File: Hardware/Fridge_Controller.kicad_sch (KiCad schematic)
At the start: 21 parts, among them J1 Power, J2 Compressor, J3 Temperature, K1 RZ01-1A4-D005, Q1 DMG3414U, U1 PIC12F683-IP, U2 MCP1541-TT

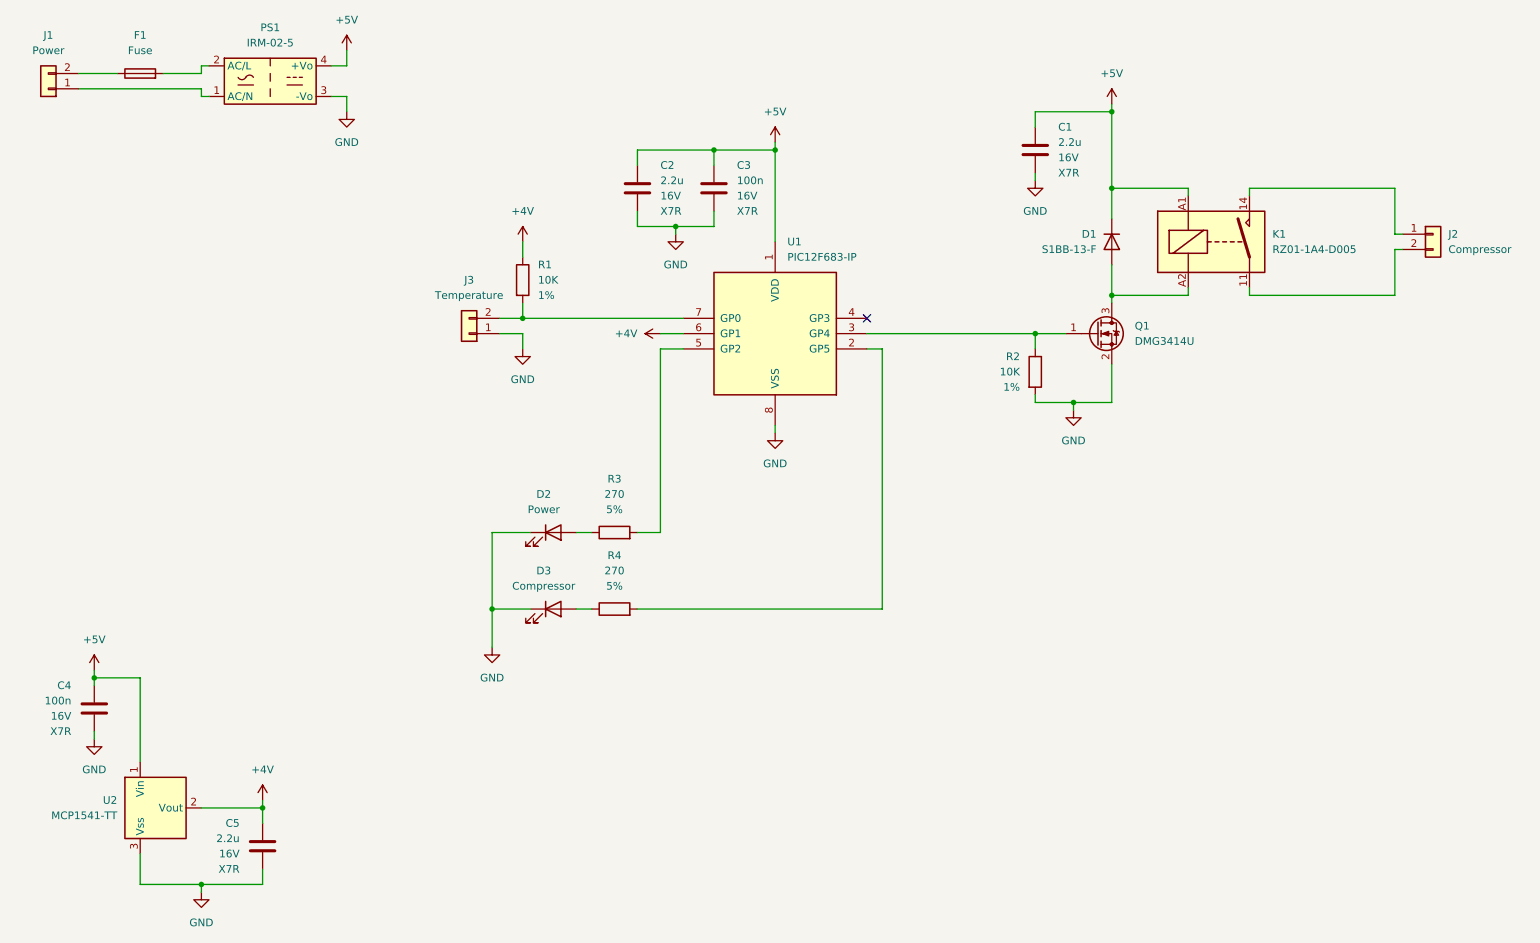
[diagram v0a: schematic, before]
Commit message: [Hardware] Added fuse, fuse holder and screw terminals part references to schematics.
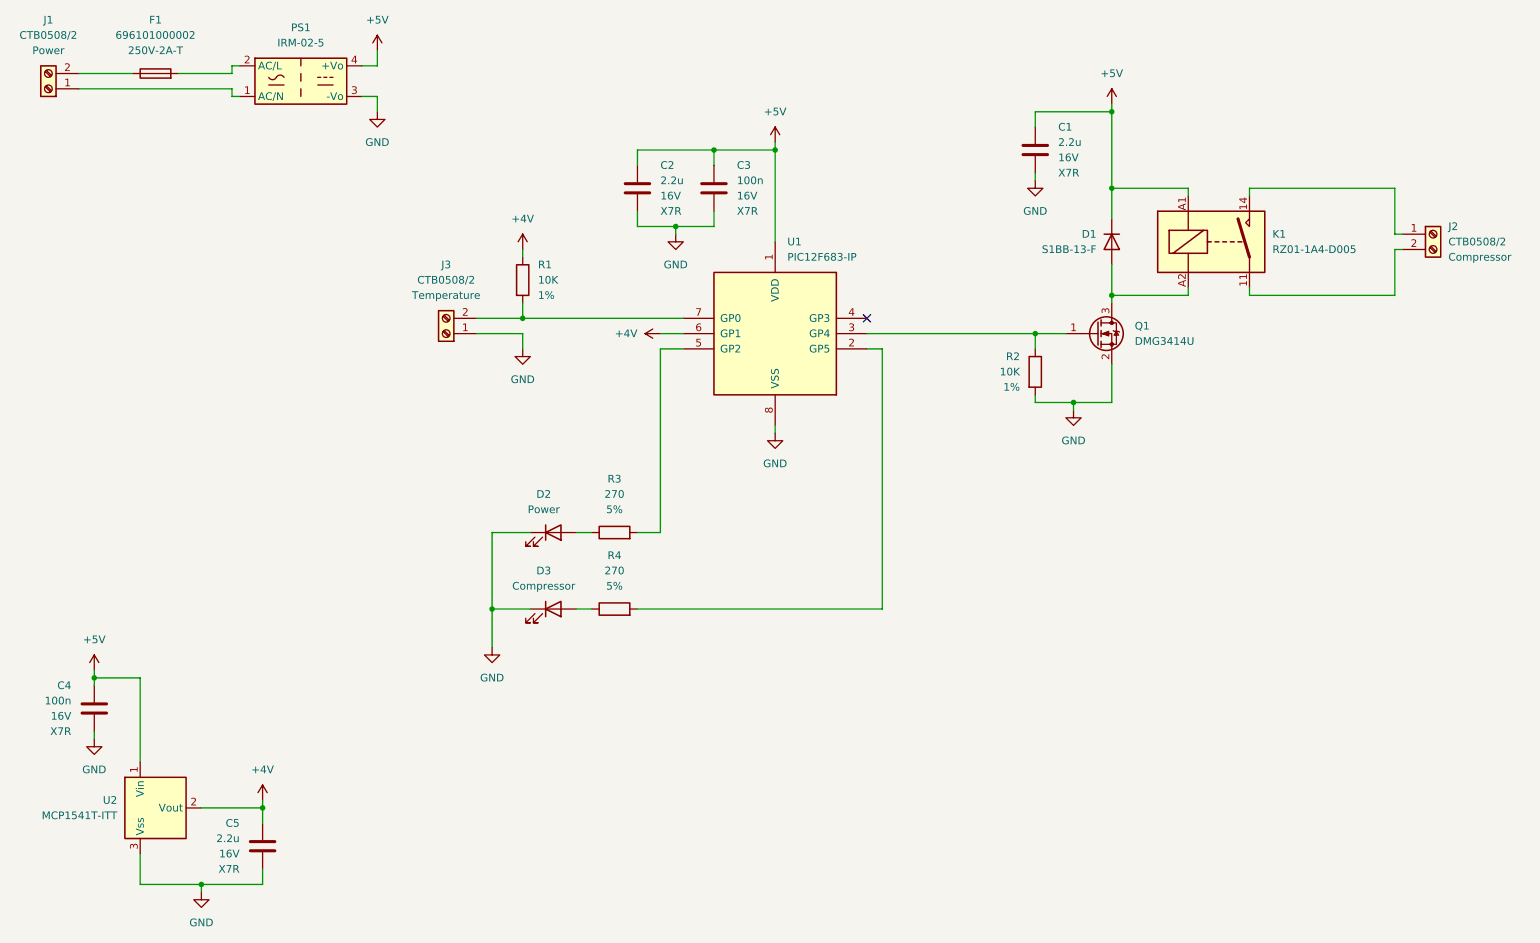
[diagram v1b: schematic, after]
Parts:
- F1: value Fuse -> 696101000002; footprint (none) -> Fuse:Fuseholder_Cylinder-5x20mm_Stelvio-Kontek_PTF78_Horizontal_Open; Manufacturer (none) -> Wurth; Value2 (none) -> 250V-2A-T
- J1: value Power -> CTB0508/2; symbol Connector_Generic:Conn_01x02 -> Connector:Screw_Terminal_01x02; Manufacturer (none) -> Camdenboss; Value2 (none) -> Power
- J2: value Compressor -> CTB0508/2; symbol Connector_Generic:Conn_01x02 -> Connector:Screw_Terminal_01x02; Manufacturer (none) -> Camdenboss; Value2 (none) -> Compressor
- J3: value Temperature -> CTB0508/2; symbol Connector_Generic:Conn_01x02 -> Connector:Screw_Terminal_01x02; Manufacturer (none) -> Camdenboss; Value2 (none) -> Temperature
- U2: value MCP1541-TT -> MCP1541T-ITT
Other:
- moved on the sheet: F1, PS1

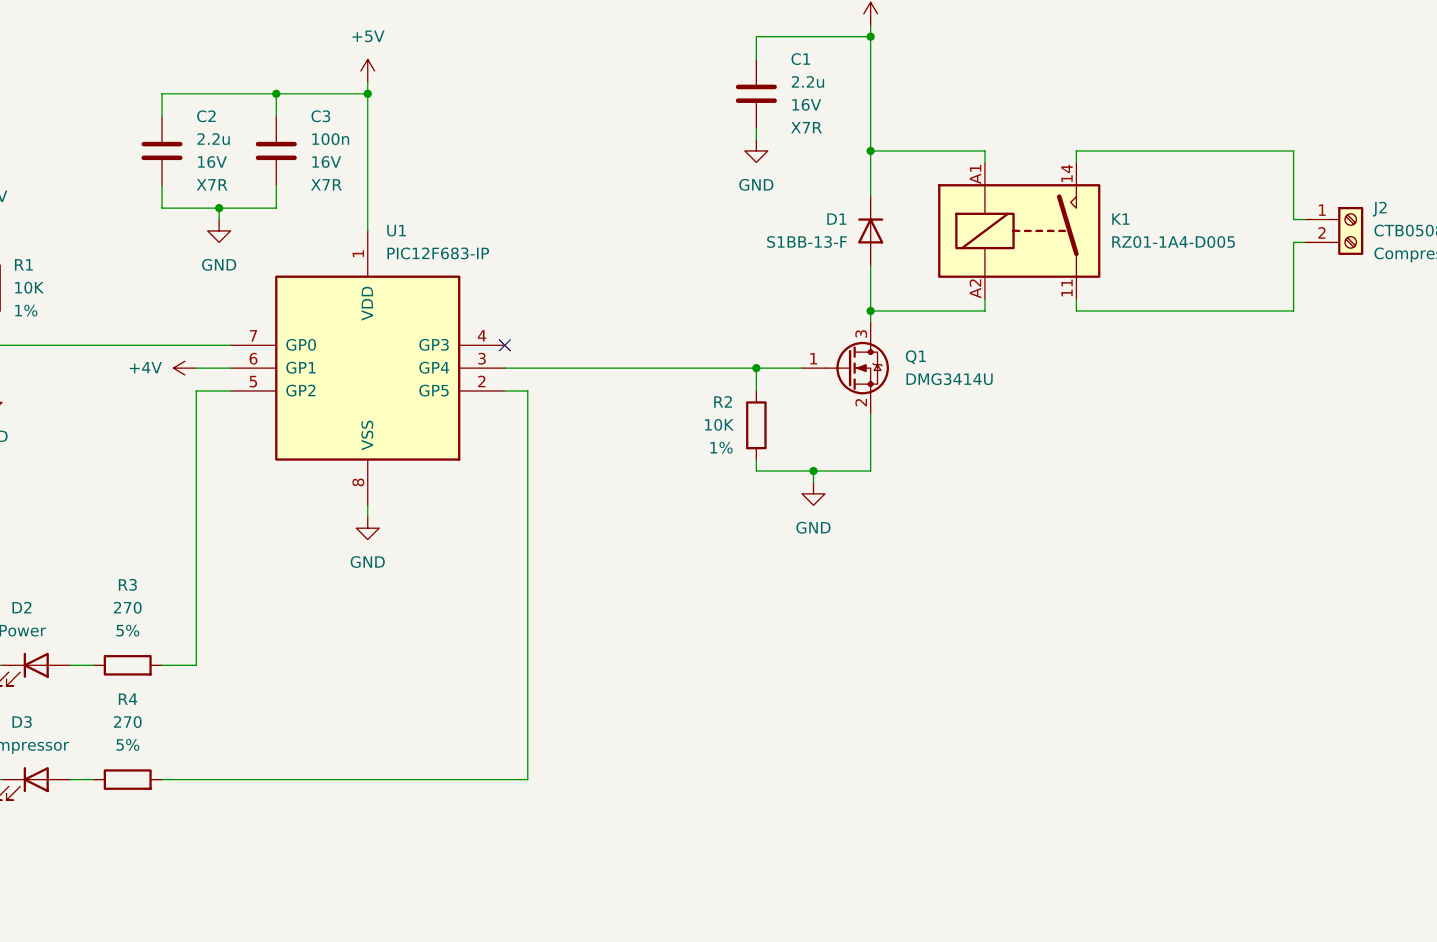
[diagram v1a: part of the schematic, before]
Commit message: [Hardware] Added a pull-up resistor on microcontroller /MCLR pin so the /MCLR signal can be left active in the MCU fuses and the MCU can be more easily reflashed when inserted on a development board.
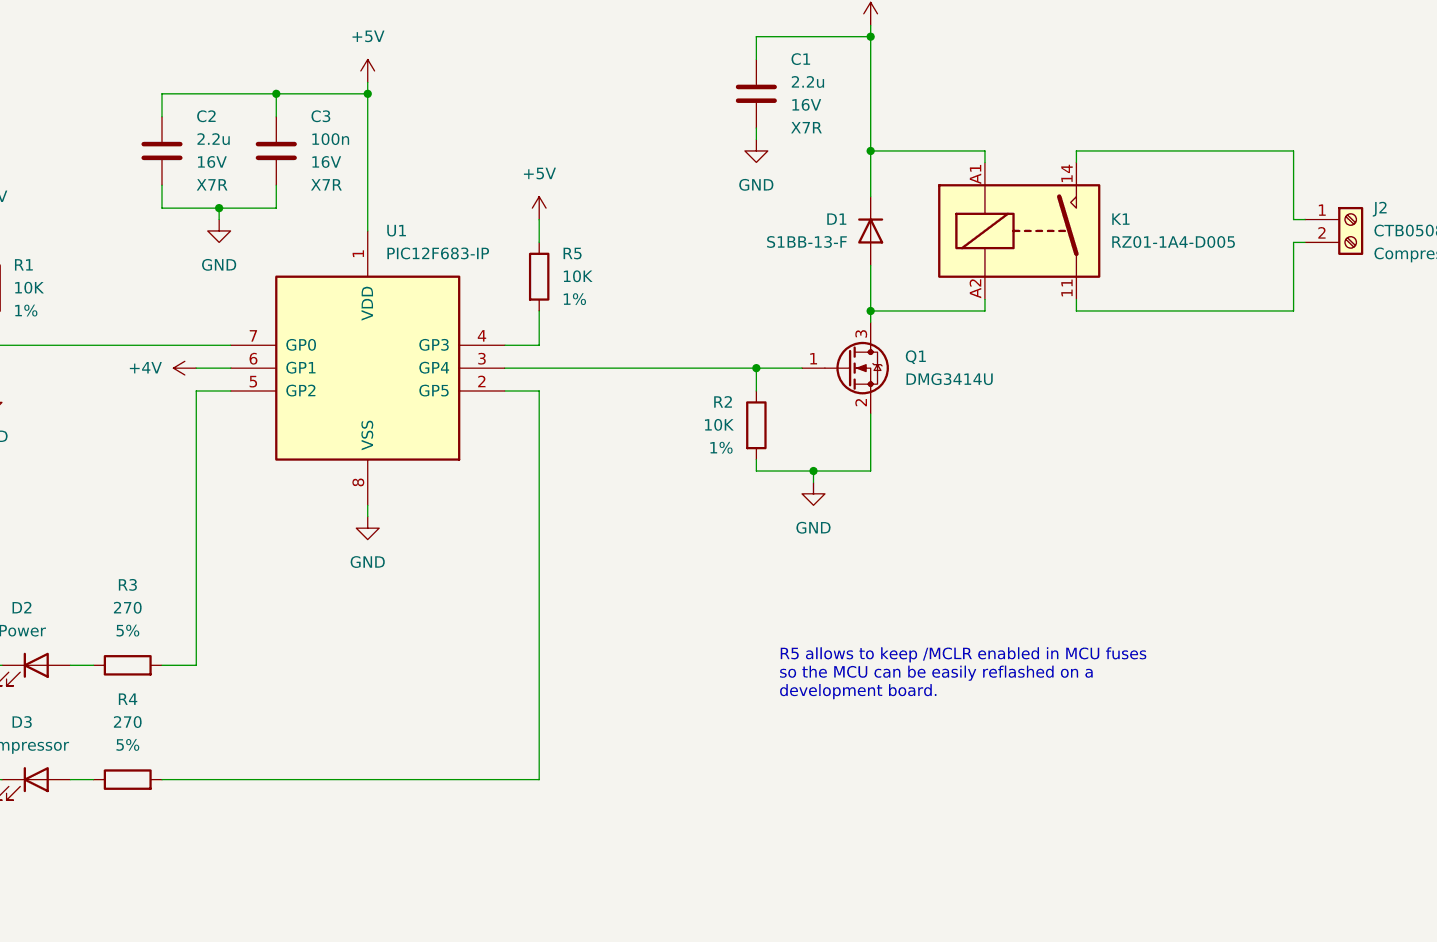
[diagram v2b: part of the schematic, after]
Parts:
- added R5: 10K, Resistor_SMD:R_0603_1608Metric_Pad0.98x0.95mm_HandSolder, symbol Device:R
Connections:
- net +5V: now also R5.1
- net at U1.4 (GP3): now also R5.2
- no-connect marks 1 -> 0
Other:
- note added: "R5 allows to keep /MCLR enabled in MCU fuses so the MCU can be easily reflashed on a development board."
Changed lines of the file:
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@@
   (junction (at 147.32 54.61) (diameter 0) (color 0 0 0 0)
   )
-  (no_connect (at 162.56 82.55))
   (wire (pts (xy 190.5 58.42) (xy 190.5 59.69))
     (stroke (width 0) (type default) (color 0 0 0 0))
@@
     (stroke (width 0) (type default) (color 0 0 0 0))
   )
-  (wire (pts (xy 162.56 87.63) (xy 165.1 87.63))
+  (wire (pts (xy 162.56 87.63) (xy 166.37 87.63))
     (stroke (width 0) (type default) (color 0 0 0 0))
   )
@@
     (stroke (width 0) (type default) (color 0 0 0 0))
   )
-  (wire (pts (xy 124.46 130.81) (xy 165.1 130.81))
+  (wire (pts (xy 124.46 130.81) (xy 166.37 130.81))
     (stroke (width 0) (type default) (color 0 0 0 0))
   )
@@
     (stroke (width 0) (type default) (color 0 0 0 0))
   )
-  (wire (pts (xy 165.1 87.63) (xy 165.1 130.81))
+  (wire (pts (xy 166.37 87.63) (xy 166.37 130.81))
     (stroke (width 0) (type default) (color 0 0 0 0))
   )
@@
     (stroke (width 0) (type default) (color 0 0 0 0))
   )
+  (wire (pts (xy 166.37 82.55) (xy 166.37 78.74))
+    (stroke (width 0) (type default) (color 0 0 0 0))
+  )
   (wire (pts (xy 100.33 118.11) (xy 106.68 118.11))
     (stroke (width 0) (type default) (color 0 0 0 0))
@@
     (stroke (width 0) (type default) (color 0 0 0 0))
   )
+  (wire (pts (xy 162.56 82.55) (xy 166.37 82.55))
+    (stroke (width 0) (type default) (color 0 0 0 0))
+  )
   (wire (pts (xy 78.74 40.64) (xy 81.28 40.64))
     (stroke (width 0) (type default) (color 0 0 0 0))
@@
     (stroke (width 0) (type default) (color 0 0 0 0))
   )
+  (wire (pts (xy 166.37 68.58) (xy 166.37 71.12))
+    (stroke (width 0) (type default) (color 0 0 0 0))
+  )
   (wire (pts (xy 57.15 44.45) (xy 57.15 45.72))
     (stroke (width 0) (type default) (color 0 0 0 0))
@@
   (wire (pts (xy 52.07 163.83) (xy 62.23 163.83))
     (stroke (width 0) (type default) (color 0 0 0 0))
+  )
+  (text "R5 allows to keep /MCLR enabled in MCU fuses\nso the MCU can be easily reflashed on a\ndevelopment board."
+    (at 193.04 121.92 0)
+    (effects (font (size 1.27 1.27)) (justify left bottom))
   )
   (symbol (lib_id "Device:C") (at 124.46 60.96 0) (unit 1)
@@
     )
     (pin "1")
+  )
+  (symbol (lib_id "Device:R") (at 166.37 74.93 0) (unit 1)
+    (in_bom yes) (on_board yes) (fields_autoplaced)
+    (property "Reference" "R5" (id 0) (at 168.91 72.3899 0)
+      (effects (font (size 1.27 1.27)) (justify left))
+    )
+    (property "Value" "10K" (id 1) (at 168.91 74.9299 0)
+      (effects (font (size 1.27 1.27)) (justify left))
+    )
+    (property "Footprint" "Resistor_SMD:R_0603_1608Metric_Pad0.98x0.95mm_HandSolder" (id 2) (at 164.592 74.93 90)
+      (effects (font (size 1.27 1.27)) hide)
+    )
+    (property "Datasheet" "~" (id 3) (at 166.37 74.93 0)
+      (effects (font (size 1.27 1.27)) hide)
+    )
+    (property "Value2" "1%" (id 4) (at 168.91 77.4699 0)
+      (effects (font (size 1.27 1.27)) (justify left))
+    )
+    (pin "1")
+    (pin "2")
   )
   (symbol (lib_id "Device:R") (at 190.5 91.44 0) (unit 1)
@@
     (pin "1")
     (pin "2")
+  )
+  (symbol (lib_id "power:+5V") (at 166.37 68.58 0) (unit 1)
+    (in_bom yes) (on_board yes) (fields_autoplaced)
+    (property "Reference" "#PWR01" (id 0) (at 166.37 72.39 0)
+      (effects (font (size 1.27 1.27)) hide)
+    )
+    (property "Value" "+5V" (id 1) (at 166.37 63.5 0))
+    (property "Footprint" "" (id 2) (at 166.37 68.58 0)
+      (effects (font (size 1.27 1.27)) hide)
+    )
+    (property "Datasheet" "" (id 3) (at 166.37 68.58 0)
+      (effects (font (size 1.27 1.27)) hide)
+    )
+    (pin "1")
   )
   (symbol (lib_id "Converter_ACDC:IRM-02-5") (at 68.58 43.18 0) (unit 1)
@@
   )
   (symbol_instances
+    (path "/4cba5240-bbb9-47df-8bed-c5548122f528"
+      (reference "#PWR01") (unit 1) (value "+5V") (footprint "")
+    )
     (path "/2e82a005-a28c-45e5-b3b4-ae7225d13bf6"
       (reference "#PWR0101") (unit 1) (value "GND") (footprint "")
@@
       (reference "R4") (unit 1) (value "270") (footprint "Resistor_SMD:R_1206_3216Metric_Pad1.30x1.75mm_HandSolder")
     )
+    (path "/20a2bbe6-b921-47a7-81a9-8c0dff82e827"
+      (reference "R5") (unit 1) (value "10K") (footprint "Resistor_SMD:R_0603_1608Metric_Pad0.98x0.95mm_HandSolder")
+    )
     (path "/5ffe612d-4bfb-491c-8802-89e93372aaa8"
